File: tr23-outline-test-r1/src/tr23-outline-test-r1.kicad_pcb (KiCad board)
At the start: 2 copper layers, 111.2 x 142.3 mm, 74 parts, among them J1 Conn_02x03_Counter_Clockwise, SW1 REV_TACT, SW10 REV_TACT, SW11 REV_TACT, SW12 REV_TACT, SW13 REV_TACT, SW14 REV_TACT, SW15 REV_TACT, SW16 REV_TACT, SW17 REV_TACT, SW18 REV_TACT, SW19 REV_TACT, SW2 REV_TACT, SW20 REV_TACT, SW21 REV_TACT, SW22 REV_TACT, SW23 REV_TACT, SW24 REV_TACT, SW25 REV_TACT, SW26 REV_TACT, SW27 REV_TACT, SW28 REV_TACT, SW29 REV_TACT, SW3 REV_TACT, SW30 REV_TACT, SW31 REV_TACT, SW32 REV_TACT, SW33 REV_TACT, SW34 REV_TACT, SW35 SW_MEC_5E, SW36 SW_MEC_5E, SW37 SW_MEC_5E, SW4 REV_TACT, SW5 REV_TACT, SW6 REV_TACT, SW7 REV_TACT, SW8 REV_TACT, SW9 REV_TACT

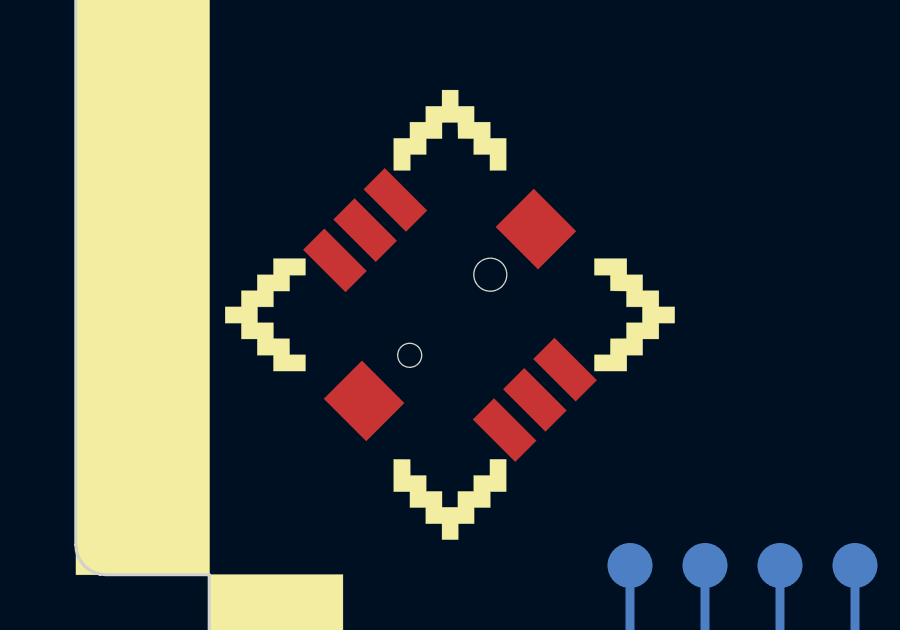
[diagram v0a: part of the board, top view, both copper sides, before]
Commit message: Route missing track for nav switch
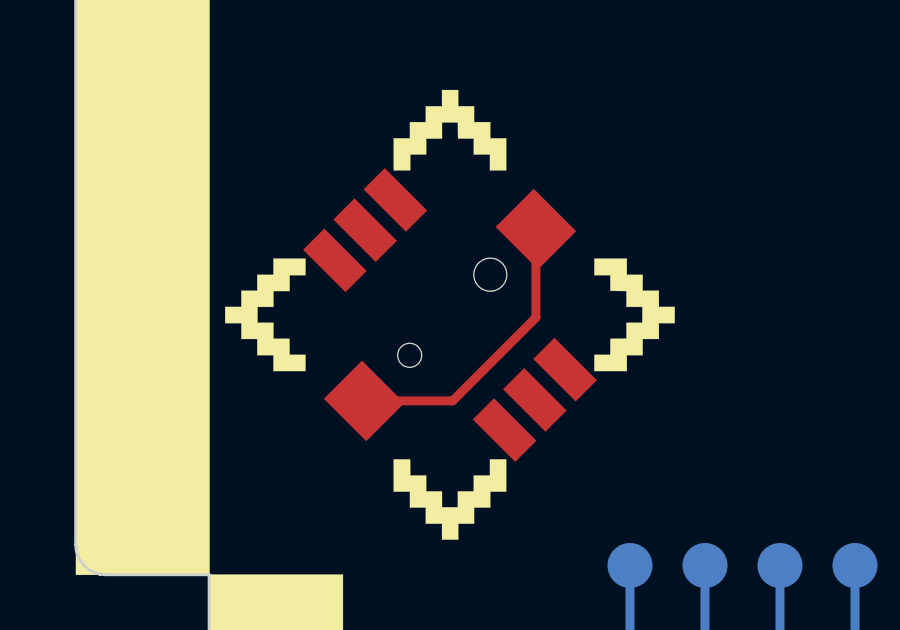
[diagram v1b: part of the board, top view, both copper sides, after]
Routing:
- net unconnected-(S1-SHIELD-PadSH1): track 0.00 -> 9.83 mm
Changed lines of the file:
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@@
   (segment (start -29.860524 4.860524) (end -29.860524 6.205456) (width 0.3) (layer "B.Cu") (net 33))
   (segment (start -20.798524 6.205456) (end -20.798524 1.798524) (width 0.3) (layer "B.Cu") (net 33))
+  (segment (start -71.363782 -42.986218) (end -68.413782 -42.986218) (width 0.3) (layer "F.Cu") (net 120))
+  (segment (start -65.636217 -45.763783) (end -65.636217 -48.713782) (width 0.3) (layer "F.Cu") (net 120))
+  (segment (start -68.413782 -42.986218) (end -65.636217 -45.763783) (width 0.3) (layer "F.Cu") (net 120))
   (zone (net 1) (net_name "GND") (layer "B.Cu") (hatch edge 0.5)
     (connect_pads (clearance 0.25))

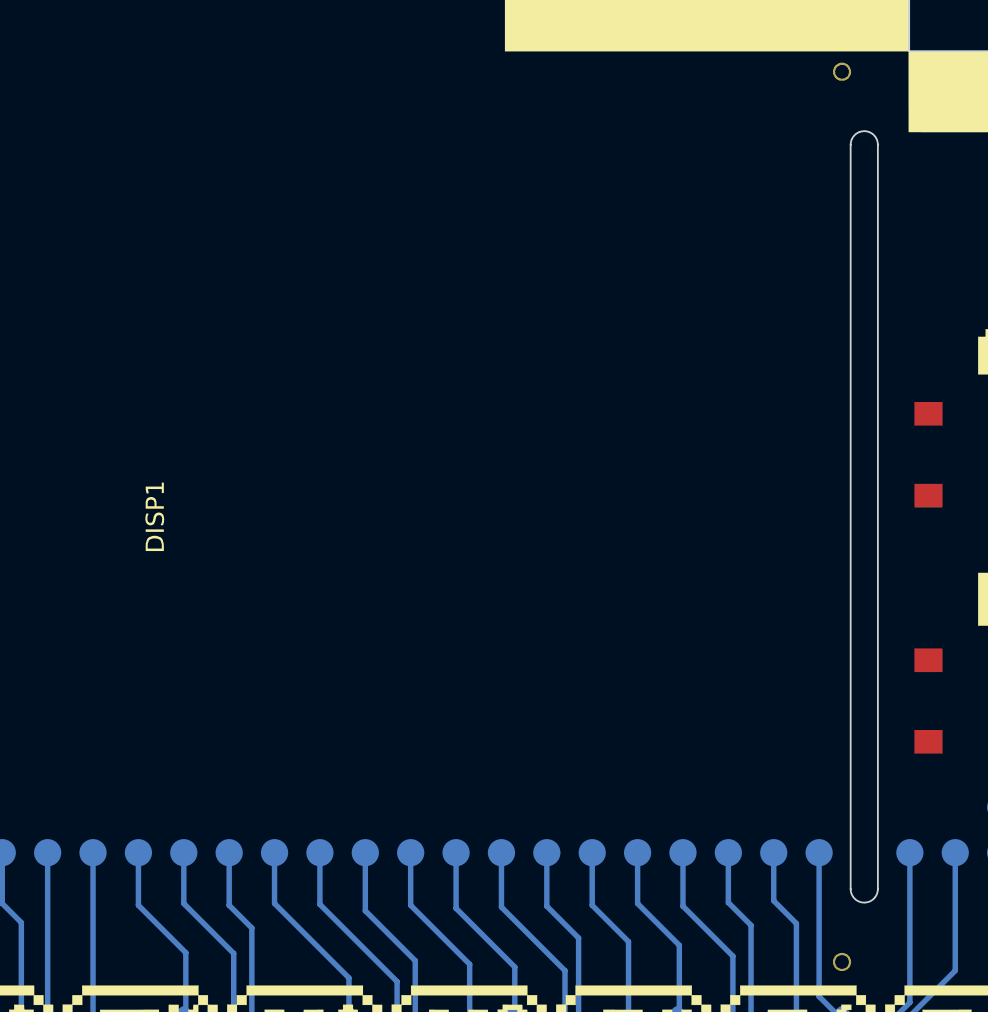
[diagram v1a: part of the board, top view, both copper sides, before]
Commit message: Add FFC connector for display.
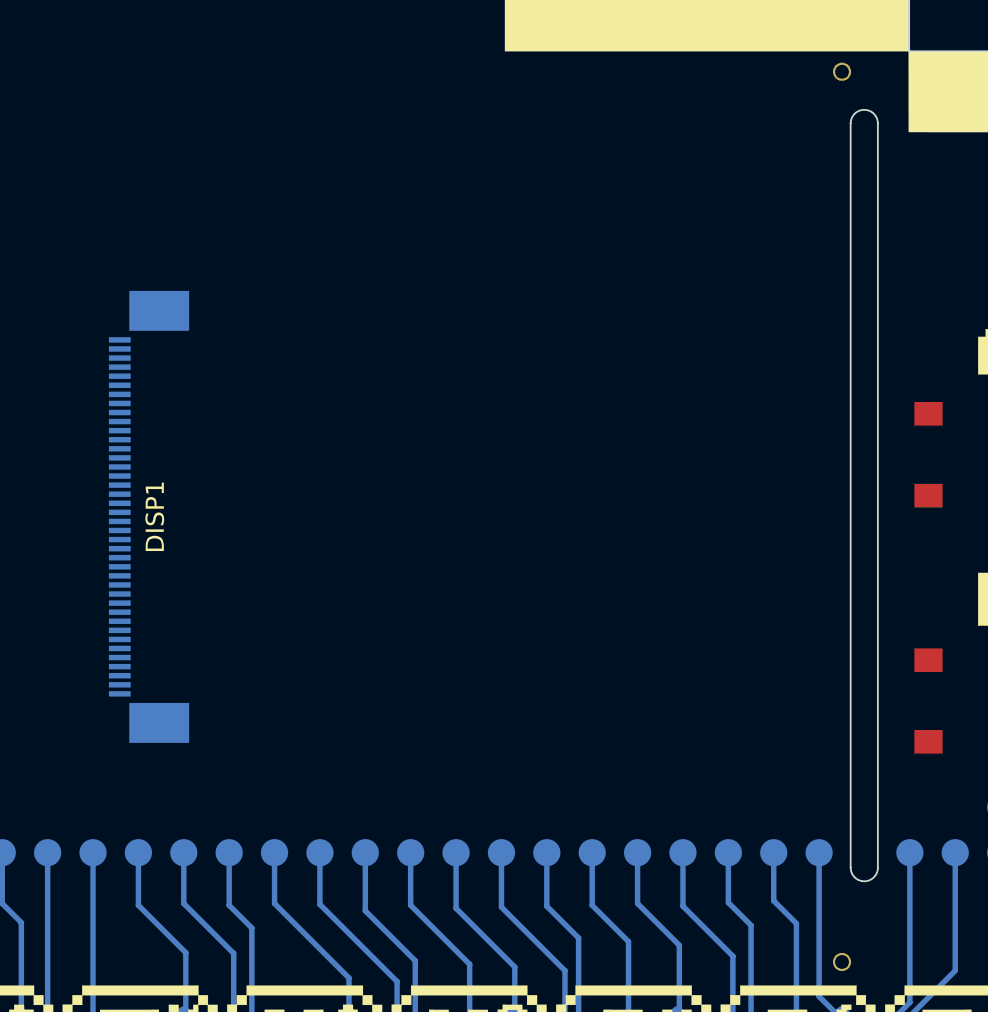
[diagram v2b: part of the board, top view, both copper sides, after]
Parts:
- added J2: Conn_01x40_MountingPin, jeffmakes-kicad-library:AFC07x40-1MP_P0.5mm_Horizontal, B.Cu at (-29.7, -56.0)

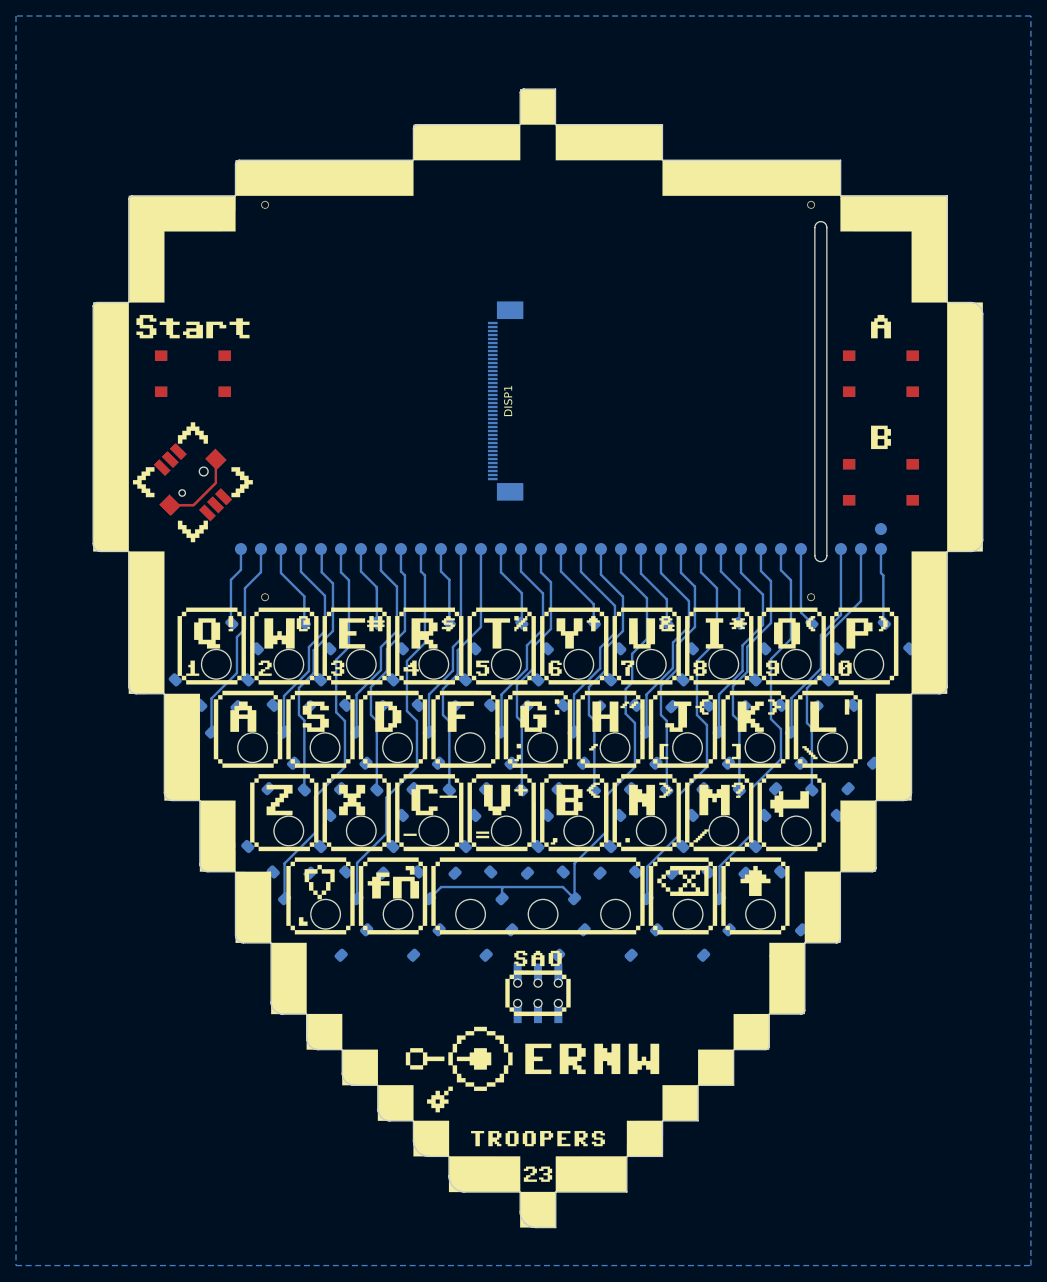
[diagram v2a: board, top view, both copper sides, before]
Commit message: Add GND pour to top layer
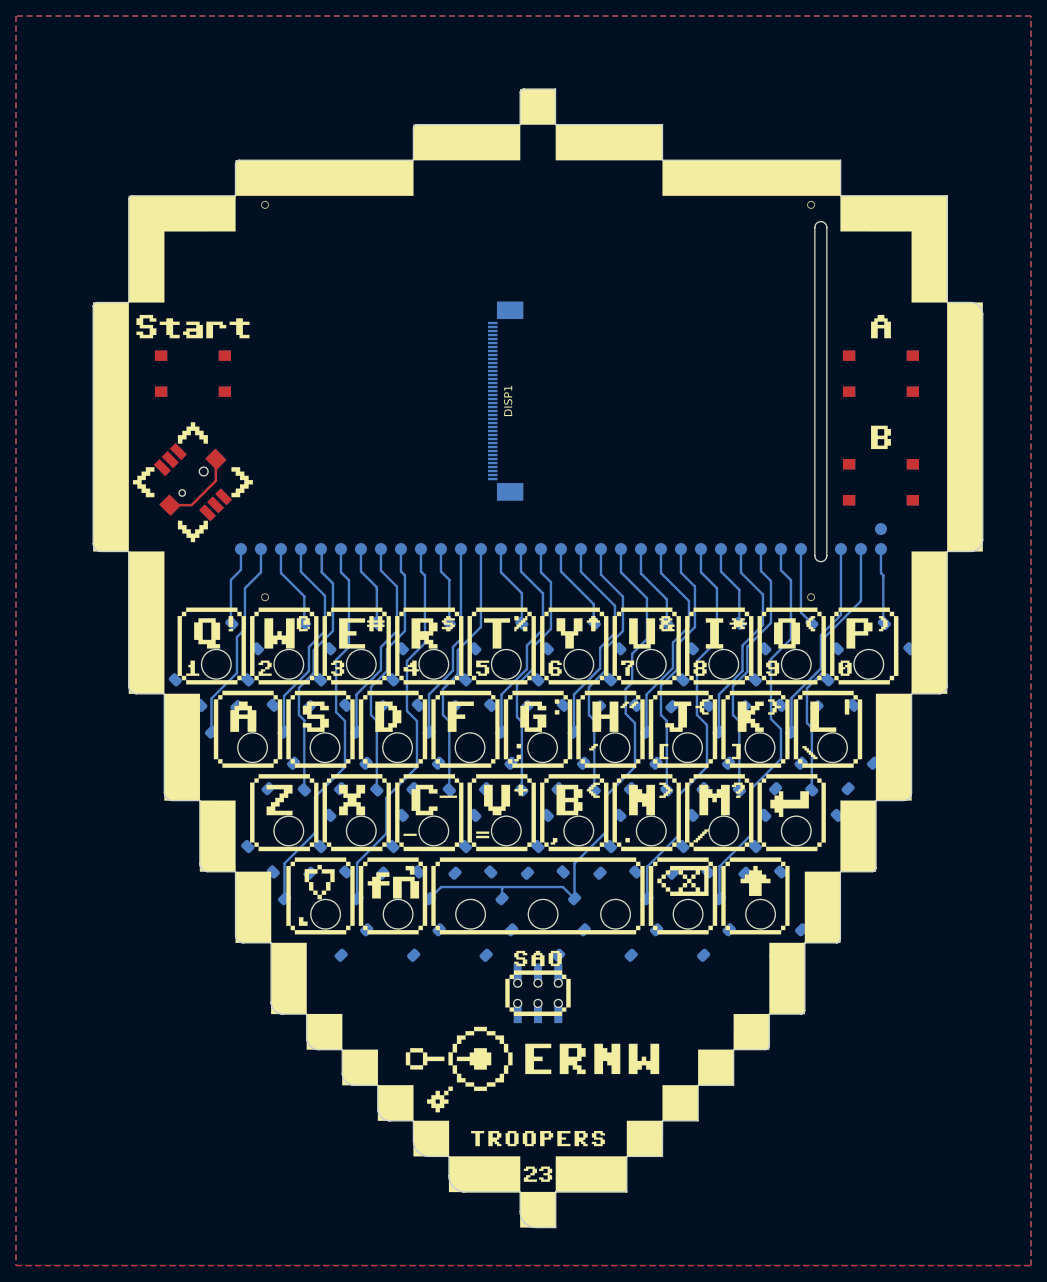
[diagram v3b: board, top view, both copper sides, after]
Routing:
- added copper zone on F.Cu, net GND
